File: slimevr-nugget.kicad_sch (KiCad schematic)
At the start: 62 parts, among them U1 nRF52840-QFXX, U3 XC6220B331MR, U4 LSM6DSV, U5 1532H, U6 QMC6309, U7 BQ24073RGT, Y1 32MHz

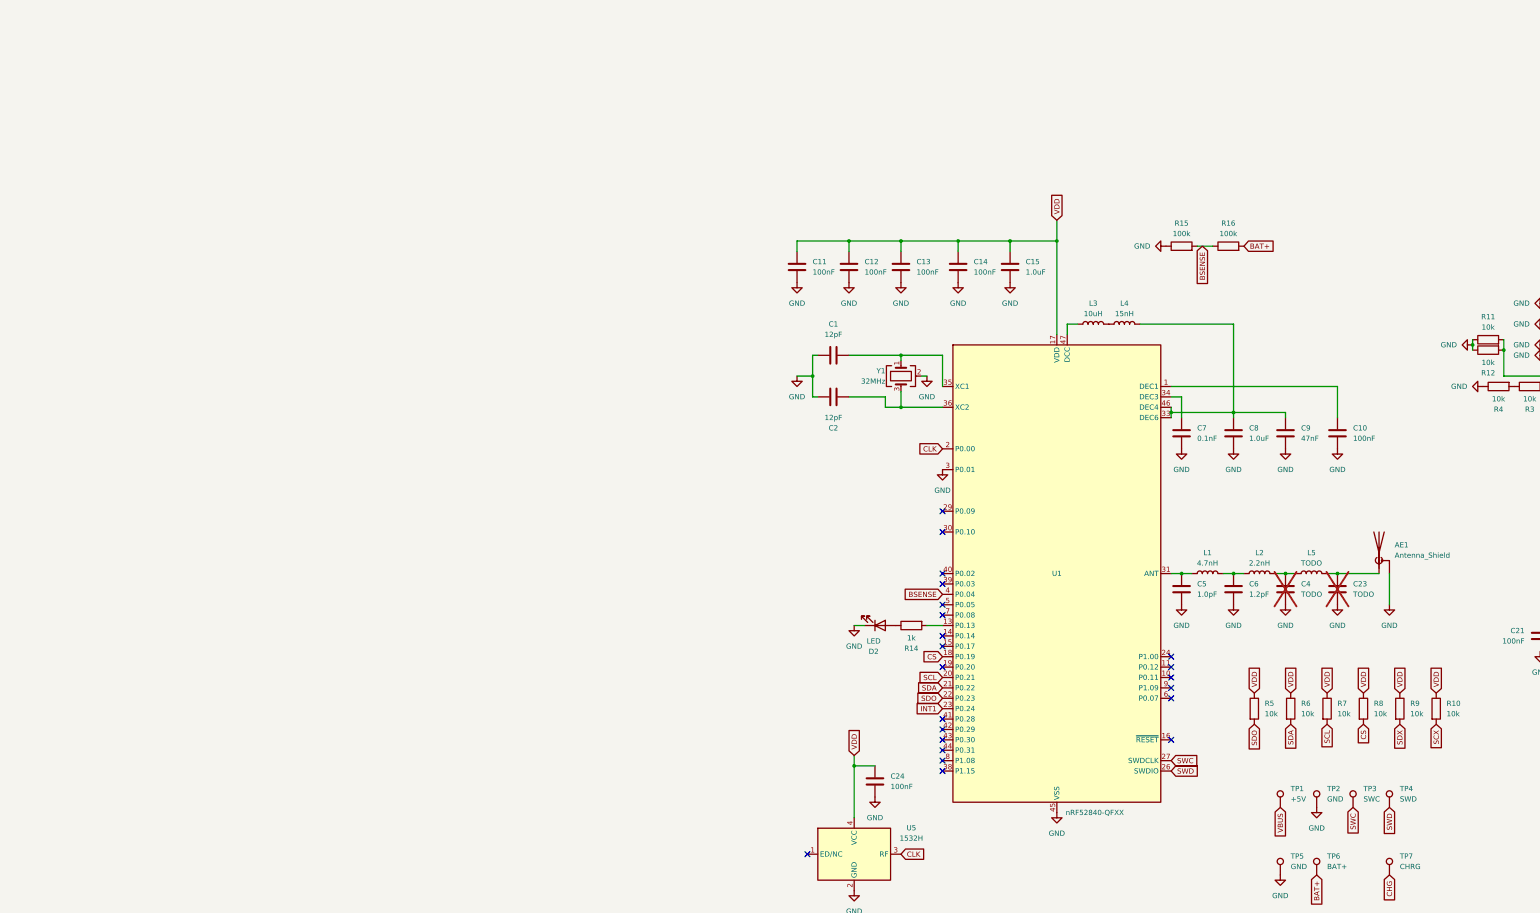
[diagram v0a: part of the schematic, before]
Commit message: Change to nRF52833, swap antenna matching circuit to IC
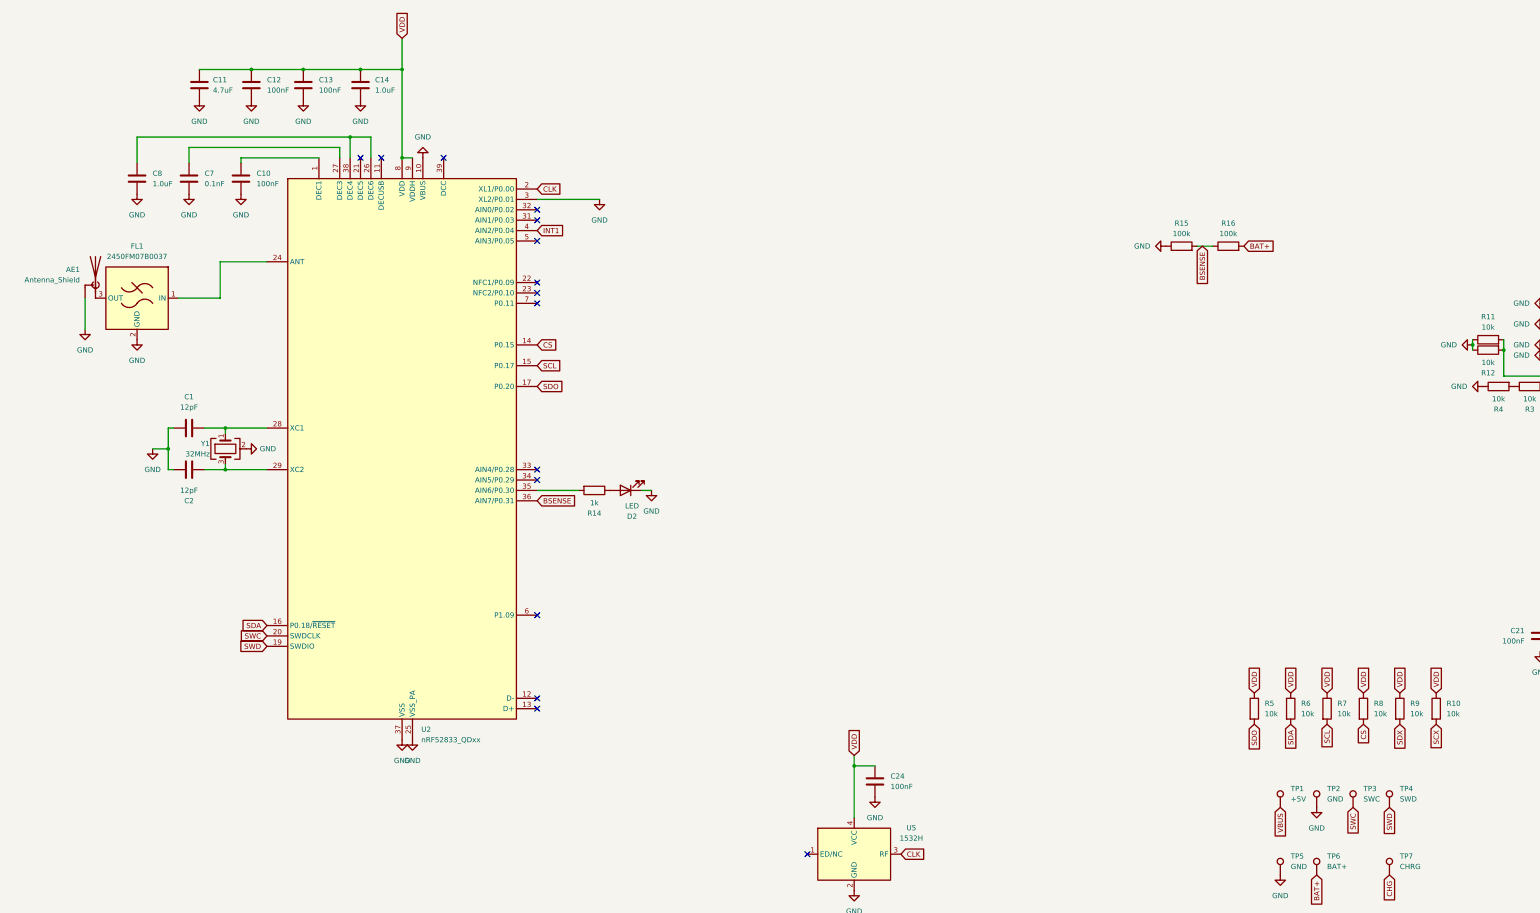
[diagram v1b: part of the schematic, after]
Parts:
- removed C15: 1.0uF, Capacitor_SMD:C_0402_1005Metric, symbol Device:C
- removed C23, C4: TODO, Capacitor_SMD:C_0402_1005Metric, symbol Device:C
- removed C5: 1.0pF, Capacitor_SMD:C_0402_1005Metric, symbol Device:C
- removed C6: 1.2pF, Capacitor_SMD:C_0402_1005Metric, symbol Device:C
- removed C9: 47nF, Capacitor_SMD:C_0402_1005Metric, symbol Device:C
- removed L1: 4.7nH, Inductor_SMD:L_0402_1005Metric, symbol Device:L
- removed L2: 2.2nH, Inductor_SMD:L_0402_1005Metric, symbol Device:L
- removed L3: 10uH, Inductor_SMD:L_0402_1005Metric, symbol Device:L
- removed L4: 15nH, Inductor_SMD:L_0402_1005Metric, symbol Device:L
- removed L5: TODO, Resistor_SMD:R_0402_1005Metric, symbol Device:L
- removed U1: nRF52840-QFXX, Package_DFN_QFN:QFN-48-1EP_6x6mm_P0.4mm_EP4.6x4.6mm_ThermalVias, symbol PCM_nordic-lib-kicad-nrf52:nRF52840-QFXX
- added FL1: 2450FM07B0037, 2450FM07B0037:2450FM07B0037, symbol RF_Filter:LFCN-2400
- added U2: nRF52833_QDxx, Package_DFN_QFN:QFN-40-1EP_5x5mm_P0.4mm_EP3.6x3.6mm, symbol MCU_Nordic:nRF52833_QDxx
- C11: value 100nF -> 4.7uF
- C14: value 100nF -> 1.0uF
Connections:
- net BSENSE: now also U2.36 (AIN7/P0.31)
- net CLK: now also U2.2 (XL1/P0.00)
- net CS: now also U2.14 (P0.15)
- net GND: now also FL1.2 (GND), FL1.4 (GND), U2.10 (VBUS), U2.25 (VSS_PA), U2.3 (XL2/P0.01), U2.37 (VSS), U2.41 (VSS)
- net INT1: now also U2.4 (AIN2/P0.04)
- net SCL: now also U2.15 (P0.17)
- net SDA: now also U2.16 (P0.18/~{RESET})
- net SDO: now also U2.17 (P0.20)
- net SWC: now also U2.20 (SWDCLK)
- net SWD: now also U2.19 (SWDIO)
- net VDD: now also U2.18 (VDD), U2.30 (VDD), U2.40 (VDD), U2.8 (VDD), U2.9 (VDDH)
- net at AE1.1 (A): now also FL1.3 (OUT)
- net at C7.2: now also U2.27 (DEC3)
- net at C10.2: now also U2.1 (DEC1)
- net at C1.2, Y1.1: now also U2.28 (XC1)
- net at C8.2: now also U2.26 (DEC6), U2.38 (DEC4)
- net at R14.2: now also U2.35 (AIN6/P0.30)
- net at C2.2, Y1.3: now also U2.29 (XC2)
- new net: FL1.1 (IN), U2.24 (ANT)
- no-connect marks 27 -> 20
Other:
- moved on the sheet: D2, R14
